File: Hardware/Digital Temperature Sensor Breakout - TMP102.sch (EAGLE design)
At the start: 13 parts, among them U1 TMP1021:1

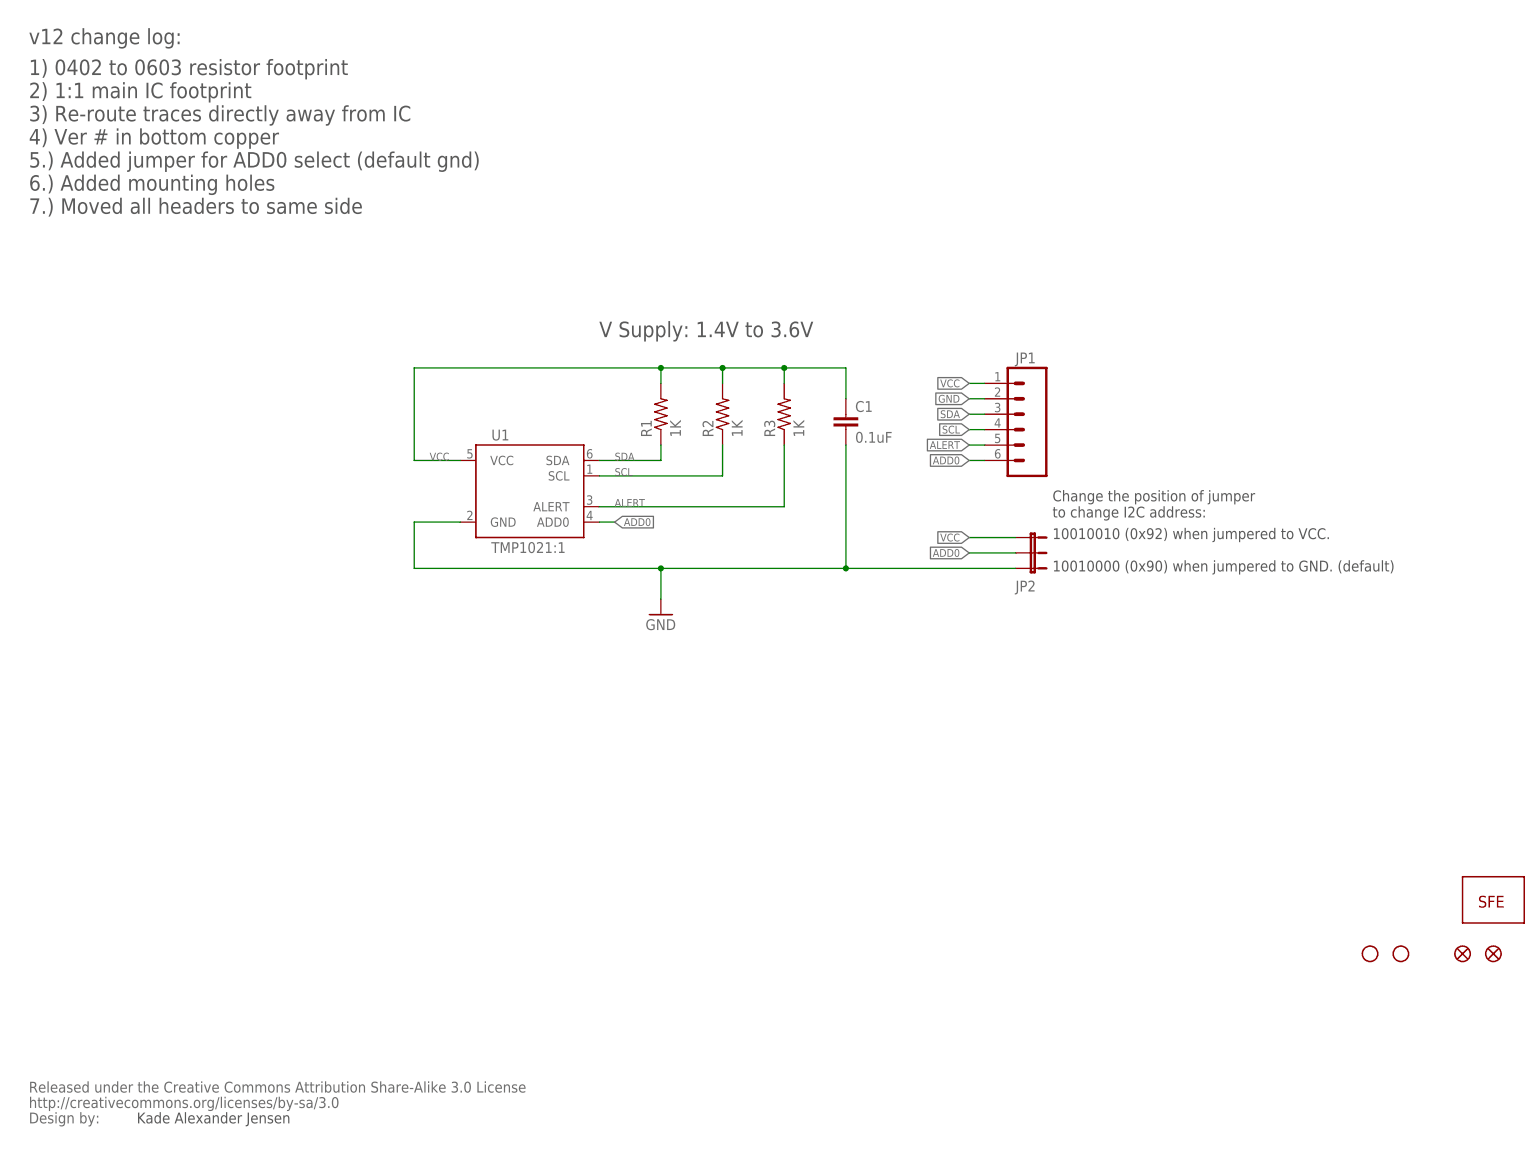
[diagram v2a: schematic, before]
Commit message: Revision 13 changes
-Changed I2C address from 0x90 to 0x48.
-Changed I2C pull-up values to 4.7k
-Changed Alert pin pull-up to 4.7k
-Added I2C pull-up solder jumper
-Changed ADD0 pull-down jumper to 2-pad NC
-Added table of I2C addresses based on ADD0 connection.
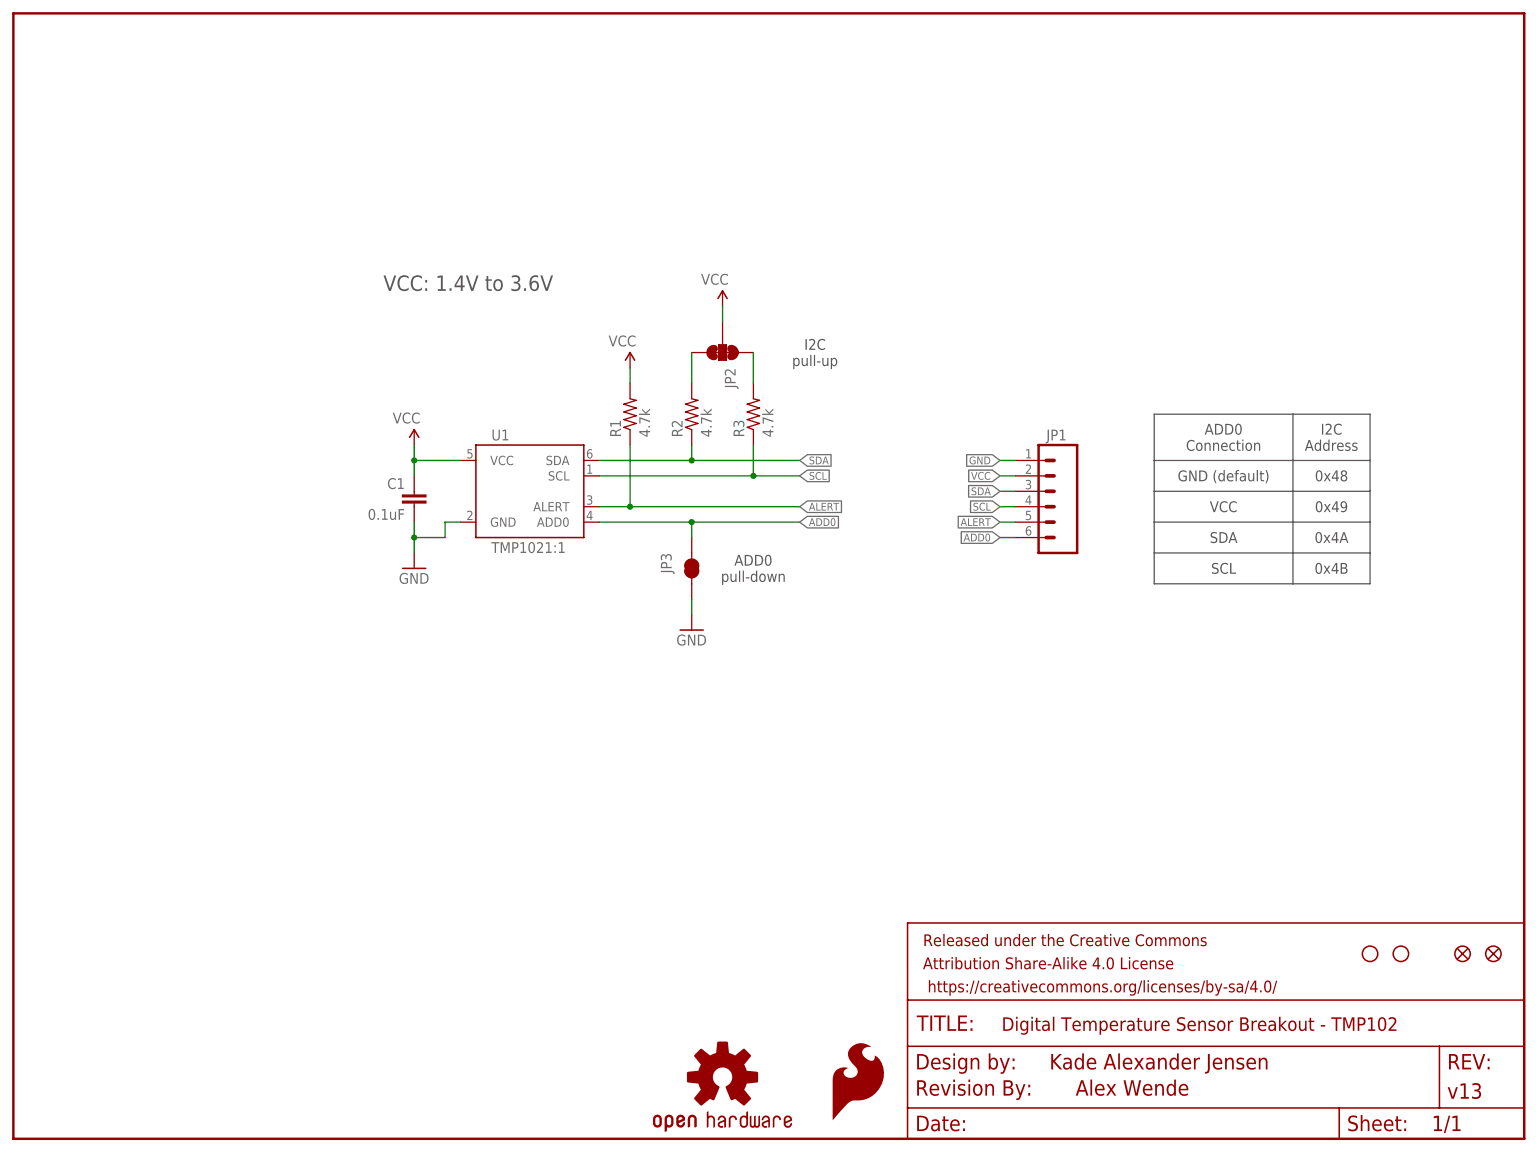
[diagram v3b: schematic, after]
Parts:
- removed JP4: FIDUCIAL1X2, SparkFun:FIDUCIAL1X2
- added FRAME2: (no value), SparkFun-Aesthetics:FRAME-LETTER
- added JP8: STAND-OFFTIGHT, SparkFun:STAND-OFFTIGHT
- added LOGO2: SFE_LOGO_FLAME.1_INCH, SparkFun-Aesthetics:SFE_LOGO_FLAME.1_INCH
- added LOGO3: OSHW-LOGOS, SparkFun-Aesthetics:OSHW-LOGOS
- JP2: value JUMPER-32-3 -> (none); device SparkFun:JUMPER-32-3 -> SparkFun-Passives:JUMPER-PAD-3-NC_BY_TRACE
- JP3: value LOGO-SFESK -> ADD0; device SparkFun:LOGO-SFESK -> SparkFun-Passives:JUMPER-PAD-2-NC_BY_TRACE
- JP6: value STAND-OFFTIGHT -> FIDUCIAL1X2; device SparkFun:STAND-OFFTIGHT -> SparkFun:FIDUCIAL1X2
- R1, R2, R3: value 1K -> 4.7k
- U$2: value CREATIVE_COMMONS -> REVISION; device SparkFun:CREATIVE_COMMONS -> SparkFun-Aesthetics:REVISION
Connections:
- new net N$1: JP2.1, R3.2
- new net N$2: JP2.3, R2.2
- net ADD0: now also JP3.1; no longer JP2.2
- net ALERT: now also R1.1; no longer R3.1
- net GND: now also JP1.1, JP3.2; no longer JP1.2, JP2.3
- net SCL: now also R3.1; no longer R2.1
- net SDA: now also R2.1; no longer R1.1
- net VCC: now also JP1.2, JP2.2; no longer JP1.1, JP2.1, R2.2, R3.2
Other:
- note added: "0x48"
- note added: "0x49"
- note added: "0x4A"
- note added: "0x4B"
- note added: "ADD0 Connection"
- note added: "ADD0 pull-down"
- note added: "Alex Wende"
- note added: "GND (default)"
- note added: "I2C Address"
- note added: "I2C pull-up"
- note added: "SCL"
- note added: "SDA"
- note added: "VCC"
- note added: "VCC: 1.4V to 3.6V"
- note removed: "1) 0402 to 0603 resistor footprint 2) 1:1 main IC footprint 3) Re-route traces directly away from IC 4) Ver # in bottom copper 5.) Added jumper for ADD0 select (default gnd) 6.) Added mounting holes 7.) Moved all headers to same side"
- note removed: "10010010 (0x92) when jumpered to VCC. 10010000 (0x90) when jumpered to GND. (default)"
- note removed: "Change the position of jumper to change I2C address:"
- note removed: "Kade Alexander Jensen"
- note removed: "V Supply: 1.4V to 3.6V"
- note removed: "v12 change log:"
- moved on the sheet: C1, JP1, R1, R2, R3

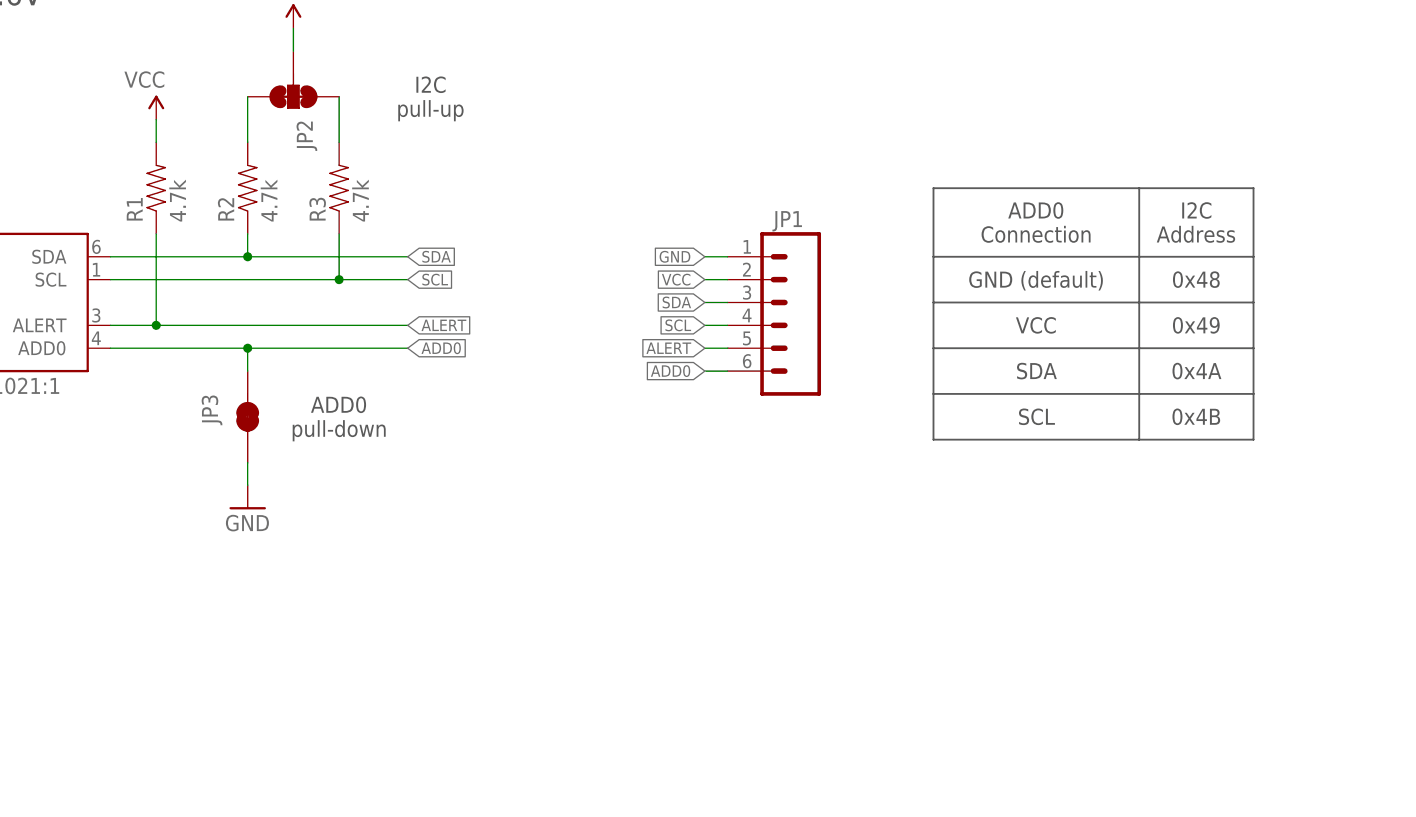
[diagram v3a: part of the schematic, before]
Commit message: Applied Fixes from Design Review
-Moved traces on end of sensors to extend out the other way.
-Added note in schematic about using an external jumper to change I2C
address.
-Removed Kade's name from document layer.
-Added pull down resistor to prevent shorts with I2C address changes.
-Added unit of measurement on Measures layer.
-Changed measurements to use 0,0 as reference.
-Removed "-" on ADD0 jumper
-Changed VCC silk on top silk to voltage range.
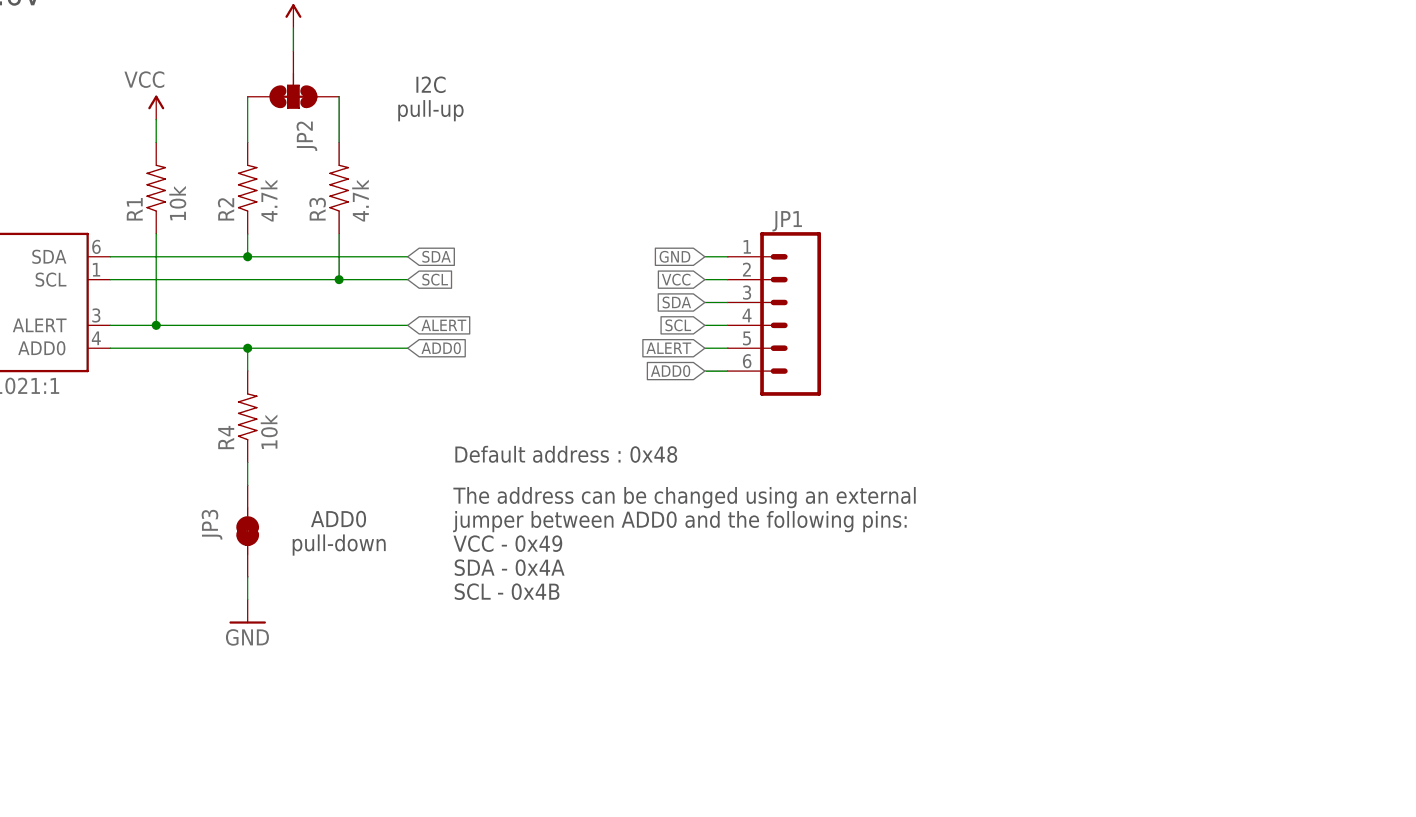
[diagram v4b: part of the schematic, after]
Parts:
- added R4: 10k, SparkFun:RESISTOR0603-RES
- R1: value 4.7k -> 10k
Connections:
- new net N$3: JP3.1, R4.1
- net ADD0: now also R4.2; no longer JP3.1
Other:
- note added: "Default address : 0x48"
- note added: "The address can be changed using an external jumper between ADD0 and the following pins: VCC - 0x49 SDA - 0x4A SCL - 0x4B"
- note removed: "0x48"
- note removed: "0x49"
- note removed: "0x4A"
- note removed: "0x4B"
- note removed: "ADD0 Connection"
- note removed: "GND (default)"
- note removed: "I2C Address"
- note removed: "SCL"
- note removed: "SDA"
- note removed: "VCC"
- moved on the sheet: JP3
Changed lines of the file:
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@@
 <setting verticaltext="up"/>
 </settings>
-<grid distance="0.1" unitdist="inch" unit="inch" style="lines" multiple="1" display="no" altdistance="0.01" altunitdist="inch" altunit="inch"/>
+<grid distance="0.1" unitdist="inch" unit="inch" style="lines" multiple="1" display="yes" altdistance="0.01" altunitdist="inch" altunit="inch"/>
 <layers>
 <layer number="1" name="Top" color="4" fill="1" visible="no" active="no"/>
@@
 <part name="R2" library="SparkFun" deviceset="RESISTOR" device="0603-RES" value="4.7k"/>
 <part name="R3" library="SparkFun" deviceset="RESISTOR" device="0603-RES" value="4.7k"/>
-<part name="R1" library="SparkFun" deviceset="RESISTOR" device="0603-RES" value="4.7k"/>
+<part name="R1" library="SparkFun" deviceset="RESISTOR" device="0603-RES" value="10k"/>
 <part name="C1" library="SparkFun" deviceset="CAP" device="0603-CAP" value="0.1uF"/>
 <part name="JP5" library="SparkFun" deviceset="FIDUCIAL" device="1X2"/>
@@
 <part name="LOGO2" library="SparkFun-Aesthetics" deviceset="SFE_LOGO_FLAME" device=".1_INCH"/>
 <part name="LOGO3" library="SparkFun-Aesthetics" deviceset="OSHW-LOGO" device="S"/>
+<part name="R4" library="SparkFun" deviceset="RESISTOR" device="0603-RES" value="10k"/>
 </parts>
 <sheets>
@@
 <text x="60.96" y="139.7" size="2.54" layer="97">VCC: 1.4V to 3.6V</text>
 <text x="175.006" y="7.112" size="2.54" layer="94">Alex Wende</text>
-<text x="199.39" y="109.22" size="1.778" layer="97" align="center">GND (default)</text>
-<wire x1="187.96" y1="111.76" x2="223.52" y2="111.76" width="0.2032" layer="97"/>
-<wire x1="223.52" y1="111.76" x2="223.52" y2="106.68" width="0.2032" layer="97"/>
-<wire x1="223.52" y1="106.68" x2="223.52" y2="101.6" width="0.2032" layer="97"/>
-<wire x1="223.52" y1="101.6" x2="223.52" y2="96.52" width="0.2032" layer="97"/>
-<wire x1="223.52" y1="96.52" x2="223.52" y2="91.44" width="0.2032" layer="97"/>
-<wire x1="223.52" y1="91.44" x2="210.82" y2="91.44" width="0.2032" layer="97"/>
-<wire x1="210.82" y1="91.44" x2="187.96" y2="91.44" width="0.2032" layer="97"/>
-<wire x1="187.96" y1="91.44" x2="187.96" y2="96.52" width="0.2032" layer="97"/>
-<text x="199.39" y="115.57" size="1.778" layer="97" align="center">ADD0
-Connection</text>
-<text x="217.17" y="115.57" size="1.778" layer="97" align="center">I2C
-Address</text>
-<wire x1="187.96" y1="96.52" x2="187.96" y2="101.6" width="0.2032" layer="97"/>
-<wire x1="187.96" y1="101.6" x2="187.96" y2="106.68" width="0.2032" layer="97"/>
-<wire x1="187.96" y1="106.68" x2="187.96" y2="111.76" width="0.2032" layer="97"/>
-<wire x1="187.96" y1="111.76" x2="187.96" y2="119.38" width="0.2032" layer="97"/>
-<wire x1="187.96" y1="119.38" x2="210.82" y2="119.38" width="0.2032" layer="97"/>
-<wire x1="210.82" y1="119.38" x2="223.52" y2="119.38" width="0.2032" layer="97"/>
-<wire x1="223.52" y1="119.38" x2="223.52" y2="111.76" width="0.2032" layer="97"/>
-<wire x1="210.82" y1="119.38" x2="210.82" y2="91.44" width="0.2032" layer="97"/>
-<wire x1="187.96" y1="106.68" x2="223.52" y2="106.68" width="0.2032" layer="97"/>
-<wire x1="223.52" y1="101.6" x2="187.96" y2="101.6" width="0.2032" layer="97"/>
-<wire x1="223.52" y1="96.52" x2="187.96" y2="96.52" width="0.2032" layer="97"/>
-<text x="199.39" y="104.14" size="1.778" layer="97" align="center">VCC</text>
-<text x="199.39" y="99.06" size="1.778" layer="97" align="center">SDA</text>
-<text x="199.39" y="93.98" size="1.778" layer="97" align="center">SCL</text>
-<text x="217.17" y="109.22" size="1.778" layer="97" align="center">0x48</text>
-<text x="217.17" y="104.14" size="1.778" layer="97" align="center">0x49</text>
-<text x="217.17" y="99.06" size="1.778" layer="97" align="center">0x4A</text>
-<text x="217.17" y="93.98" size="1.778" layer="97" align="center">0x4B</text>
-<text x="121.92" y="93.98" size="1.778" layer="97" align="center">ADD0
+<text x="121.92" y="81.28" size="1.778" layer="97" align="center">ADD0
 pull-down</text>
 <text x="132.08" y="129.54" size="1.778" layer="97" align="center">I2C
 pull-up</text>
+<text x="134.62" y="88.9" size="1.778" layer="97">Default address : 0x48</text>
+<text x="134.62" y="73.66" size="1.778" layer="97">The address can be changed using an external
+jumper between ADD0 and the following pins:
+VCC - 0x49
+SDA - 0x4A
+SCL - 0x4B</text>
 </plain>
 <instances>
@@
 </instance>
 <instance part="SUPPLY1" gate="G$1" x="66.04" y="114.3" rot="MR0"/>
-<instance part="GND1" gate="1" x="111.76" y="83.82"/>
+<instance part="GND1" gate="1" x="111.76" y="71.12"/>
 <instance part="SUPPLY2" gate="G$1" x="101.6" y="127" rot="MR0"/>
 <instance part="SUPPLY3" gate="G$1" x="116.84" y="137.16" rot="MR0"/>
 <instance part="JP2" gate="G$1" x="116.84" y="129.54" rot="R270"/>
 <instance part="U$2" gate="G$1" x="148.59" y="7.112"/>
-<instance part="JP3" gate="G$1" x="111.76" y="93.98" smashed="yes" rot="R270">
-<attribute name="NAME" x="106.68" y="96.52" size="1.778" layer="95" rot="R270"/>
+<instance part="JP3" gate="G$1" x="111.76" y="81.28" smashed="yes" rot="R270">
+<attribute name="NAME" x="106.68" y="83.82" size="1.778" layer="95" rot="R270"/>
 </instance>
 <instance part="LOGO2" gate="G$1" x="134.62" y="2.54"/>
 <instance part="LOGO3" gate="G$1" x="116.84" y="10.16"/>
+<instance part="R4" gate="G$1" x="111.76" y="93.98" rot="R90"/>
 </instances>
 <busses>
@@
 <pinref part="GND1" gate="1" pin="GND"/>
 <pinref part="JP3" gate="G$1" pin="2"/>
-<wire x1="111.76" y1="86.36" x2="111.76" y2="88.9" width="0.1524" layer="91"/>
+<wire x1="111.76" y1="73.66" x2="111.76" y2="76.2" width="0.1524" layer="91"/>
 </segment>
 <segment>
@@
 <segment>
 <pinref part="U1" gate="G$1" pin="ADD0"/>
+<label x="129.54" y="101.6" size="1.27" layer="95" xref="yes"/>
 <wire x1="96.52" y1="101.6" x2="111.76" y2="101.6" width="0.1524" layer="91"/>
-<label x="129.54" y="101.6" size="1.27" layer="95" xref="yes"/>
-<pinref part="JP3" gate="G$1" pin="1"/>
+<pinref part="R4" gate="G$1" pin="2"/>
 <wire x1="111.76" y1="101.6" x2="129.54" y2="101.6" width="0.1524" layer="91"/>
 <wire x1="111.76" y1="99.06" x2="111.76" y2="101.6" width="0.1524" layer="91"/>
@@
 </segment>
 </net>
+<net name="N$3" class="0">
+<segment>
+<pinref part="R4" gate="G$1" pin="1"/>
+<pinref part="JP3" gate="G$1" pin="1"/>
+<wire x1="111.76" y1="88.9" x2="111.76" y2="86.36" width="0.1524" layer="91"/>
+</segment>
+</net>
